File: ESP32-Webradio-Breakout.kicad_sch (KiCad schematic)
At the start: 47 parts, among them J1 AudioJack3, J2 Conn_01x01, J3 Conn_01x02, P1 USB_C_Plug, Q1 BC817, Q2 BC817, Q3 BC817, SW1 RotaryEncoder_Switch, U1 AMS1117-3.3, U2 ESP32-WROOM-32, U3 CH340C, U4 PCF8574TS, U5 DS18B20

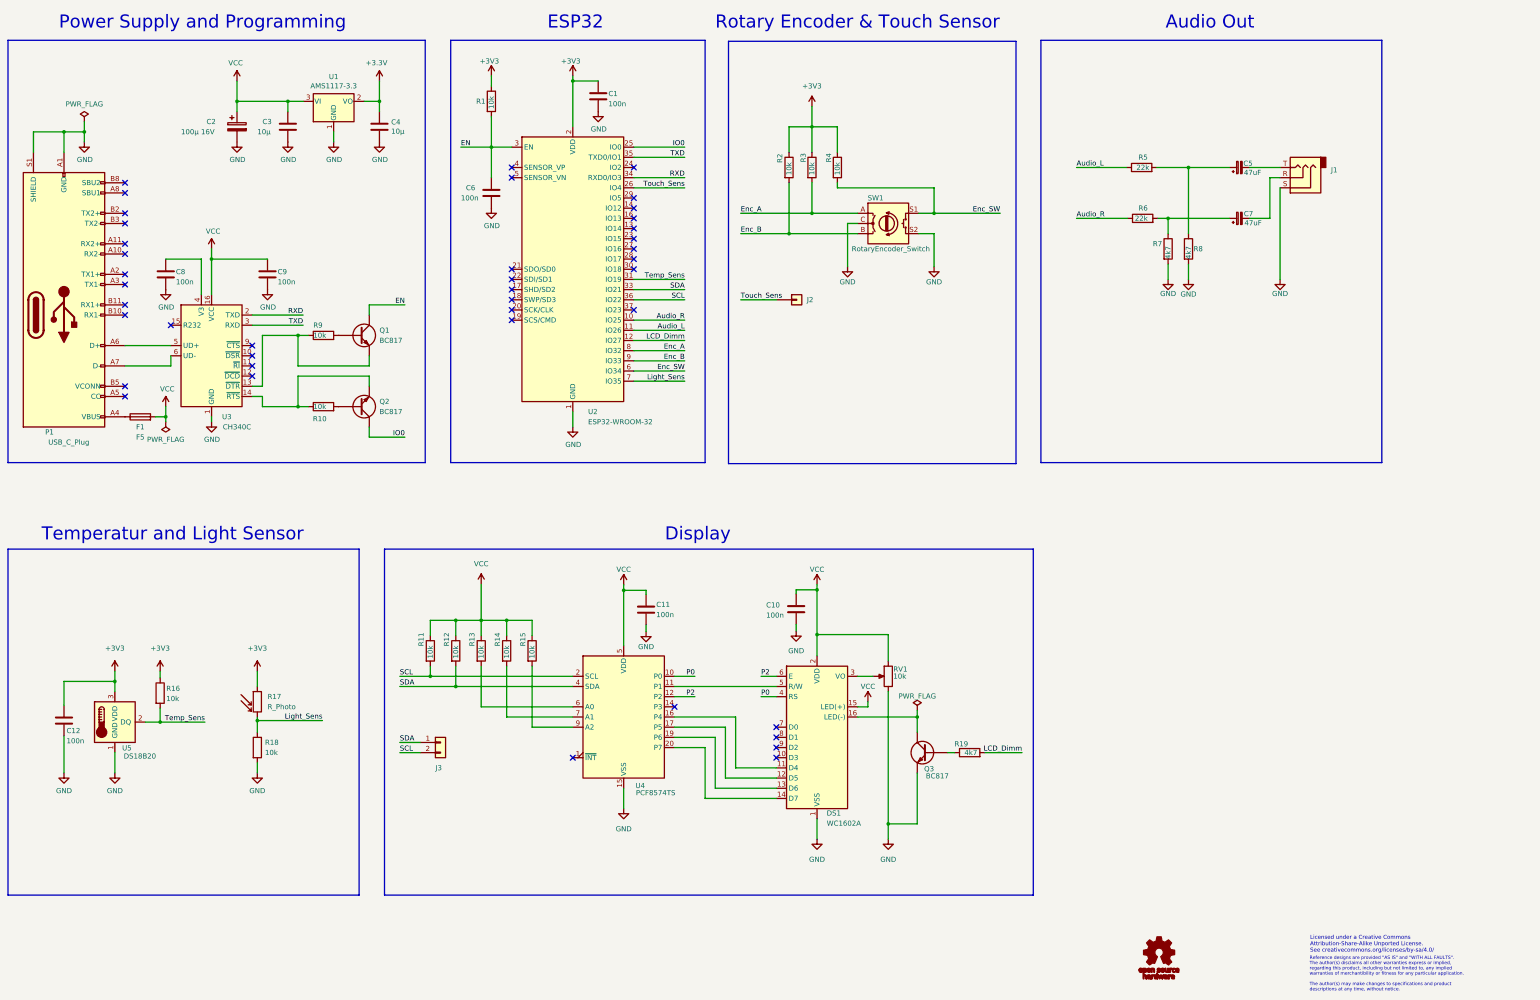
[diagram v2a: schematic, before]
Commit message: Changed USB-C symbol Added 5k1 resistors for 5V handshake
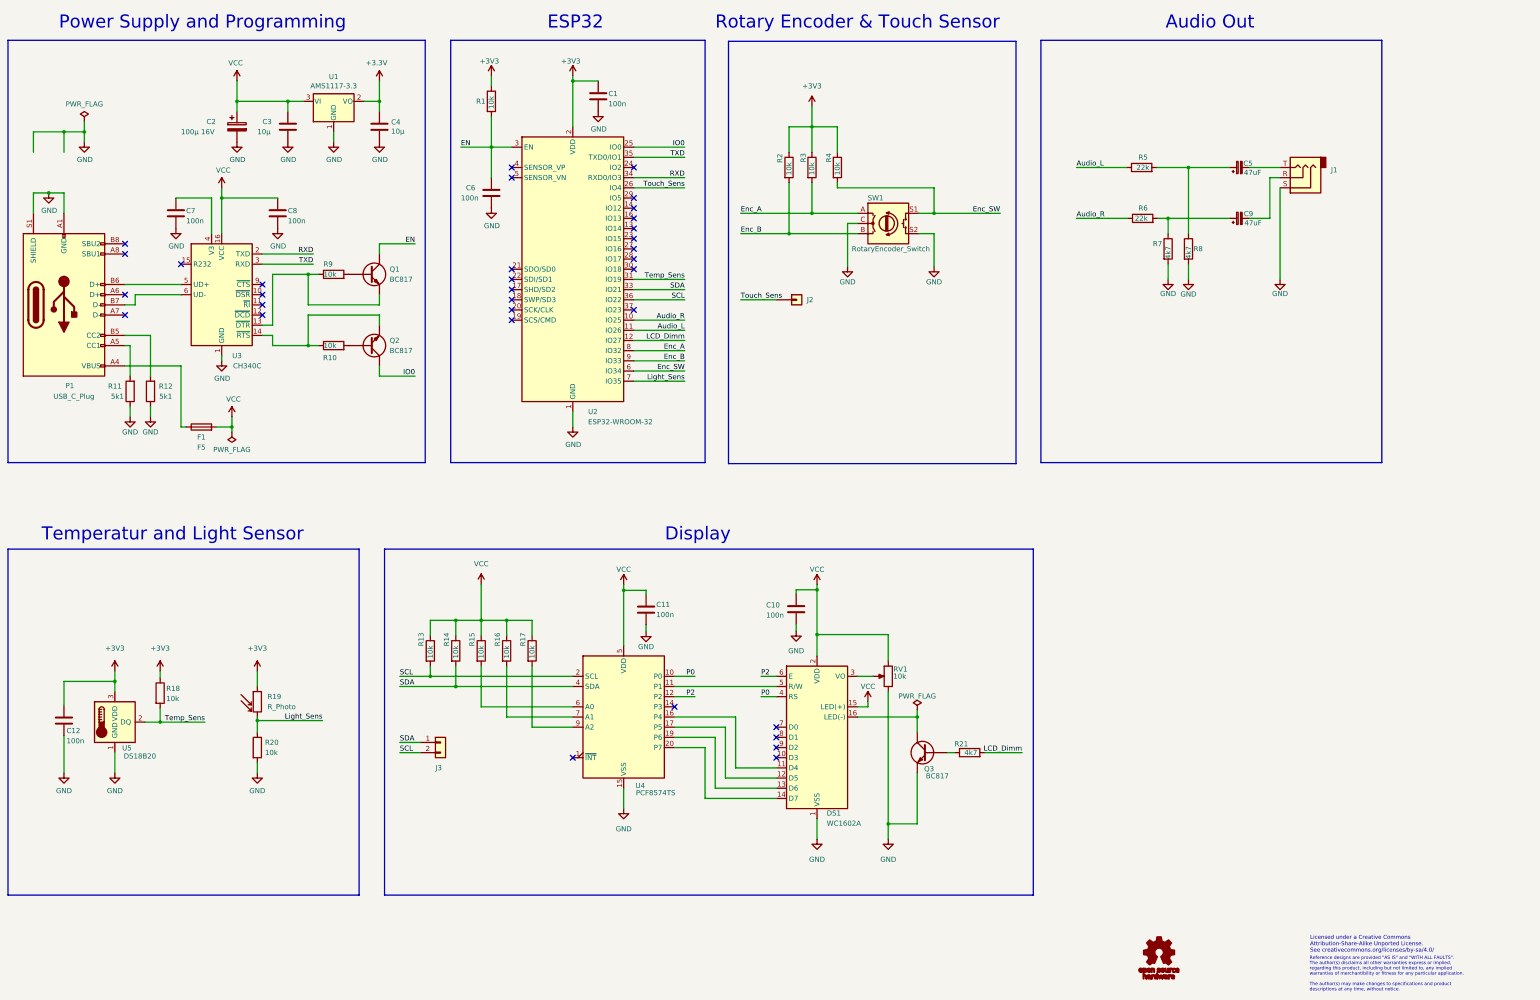
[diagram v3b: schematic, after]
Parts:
- removed P1: USB_C_Plug, Connector_USB:USB_C_Receptacle_XKB_U262-16XN-4BVC11, symbol Connector:USB_C_Plug
- added P1: USB_C_Plug, Connector_USB:USB_C_Receptacle_XKB_U262-16XN-4BVC11, symbol Connector:USB_C_Receptacle_USB2.0
- added R11, R12: 5k1, Resistor_SMD:R_0603_1608Metric, symbol Device:R
- renumbered C8 to C7, C9 to C8, C7 to C9, R11 to R13, R12 to R14, R13 to R15, R14 to R16, R15 to R17, R16 to R18, R17 to R19, R18 to R20, R19 to R21
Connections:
- net GND: now also P1.A1 (GND), P1.A12 (GND), P1.B1 (GND), P1.B12 (GND), P1.S1 (SHIELD), R11.1, R12.1
- net at F1.1: now also P1.A4 (VBUS), P1.A9 (VBUS), P1.B4 (VBUS), P1.B9 (VBUS)
- net at U3.5 (UD+): now also P1.B6 (D+)
- net at U3.6 (UD-): now also P1.B7 (D-)
- new net: P1.A5 (CC1), R11.2
- new net: P1.B5 (CC2), R12.2
- no-connect marks 41 -> 33
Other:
- moved on the sheet: C7, C8, F1, Q1, Q2, R10, R9, U3

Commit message: first routing
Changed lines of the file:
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@@
   (junction (at 149.86 175.26) (diameter 0) (color 0 0 0 0)
   )
-  (junction (at 57.15 53.34) (diameter 0) (color 0 0 0 0)
-  )
   (junction (at 95.25 45.72) (diameter 0) (color 0 0 0 0)
   )
   (junction (at 269.24 73.66) (diameter 0) (color 0 0 0 0)
-  )
-  (junction (at 52.07 53.34) (diameter 0) (color 0 0 0 0)
   )
   (junction (at 64.77 190.5) (diameter 0) (color 0 0 0 0)
@@
     (stroke (width 0) (type default) (color 0 0 0 0))
   )
+  (wire (pts (xy 48.26 61.595) (xy 48.26 68.58))
+    (stroke (width 0) (type default) (color 0 0 0 0))
+  )
   (wire (pts (xy 67.31 106.68) (xy 68.58 106.68))
     (stroke (width 0) (type default) (color 0 0 0 0))
@@
     (stroke (width 0) (type default) (color 0 0 0 0))
   )
+  (wire (pts (xy 48.26 72.39) (xy 48.26 68.58))
+    (stroke (width 0) (type default) (color 0 0 0 0))
+  )
   (wire (pts (xy 217.17 201.93) (xy 217.17 214.63))
     (stroke (width 0) (type default) (color 0 0 0 0))
@@
     (stroke (width 0) (type default) (color 0 0 0 0))
   )
-  (wire (pts (xy 57.15 53.34) (xy 57.15 55.88))
-    (stroke (width 0) (type default) (color 0 0 0 0))
-  )
   (wire (pts (xy 252.73 195.58) (xy 252.73 196.85))
     (stroke (width 0) (type default) (color 0 0 0 0))
@@
   )
   (wire (pts (xy 204.47 191.77) (xy 229.87 191.77))
-    (stroke (width 0) (type default) (color 0 0 0 0))
-  )
-  (wire (pts (xy 52.07 53.34) (xy 52.07 58.42))
     (stroke (width 0) (type default) (color 0 0 0 0))
   )
@@
     (stroke (width 0) (type default) (color 0 0 0 0))
   )
-  (wire (pts (xy 44.45 58.42) (xy 44.45 53.34))
-    (stroke (width 0) (type default) (color 0 0 0 0))
-  )
   (wire (pts (xy 135.89 189.23) (xy 143.51 189.23))
     (stroke (width 0) (type default) (color 0 0 0 0))
@@
     (stroke (width 0) (type default) (color 0 0 0 0))
   )
-  (wire (pts (xy 52.07 53.34) (xy 57.15 53.34))
-    (stroke (width 0) (type default) (color 0 0 0 0))
-  )
   (polyline (pts (xy 148.59 30.48) (xy 148.59 135.89))
     (stroke (width 0) (type default) (color 0 0 0 0))
@@
     (stroke (width 0) (type default) (color 0 0 0 0))
   )
-  (wire (pts (xy 57.15 50.8) (xy 57.15 53.34))
-    (stroke (width 0) (type default) (color 0 0 0 0))
-  )
   (wire (pts (xy 247.65 76.2) (xy 247.65 86.995))
     (stroke (width 0) (type default) (color 0 0 0 0))
@@
   )
   (wire (pts (xy 238.76 52.07) (xy 238.76 58.42))
-    (stroke (width 0) (type default) (color 0 0 0 0))
-  )
-  (wire (pts (xy 44.45 53.34) (xy 52.07 53.34))
     (stroke (width 0) (type default) (color 0 0 0 0))
   )
@@
     (pin "2")
   )
-  (symbol (lib_id "power:PWR_FLAG") (at 57.15 50.8 0) (mirror y) (unit 1)
-    (in_bom yes) (on_board yes)
-    (property "Reference" "#FLG01" (id 0) (at 57.15 48.895 0)
-      (effects (font (size 1.27 1.27)) hide)
-    )
-    (property "Value" "PWR_FLAG" (id 1) (at 57.15 46.4058 0))
-    (property "Footprint" "" (id 2) (at 57.15 50.8 0)
-      (effects (font (size 1.27 1.27)) hide)
-    )
-    (property "Datasheet" "~" (id 3) (at 57.15 50.8 0)
+  (symbol (lib_id "power:PWR_FLAG") (at 48.26 61.595 0) (mirror y) (unit 1)
+    (in_bom yes) (on_board yes)
+    (property "Reference" "#FLG01" (id 0) (at 48.26 59.69 0)
+      (effects (font (size 1.27 1.27)) hide)
+    )
+    (property "Value" "PWR_FLAG" (id 1) (at 48.26 57.2008 0))
+    (property "Footprint" "" (id 2) (at 48.26 61.595 0)
+      (effects (font (size 1.27 1.27)) hide)
+    )
+    (property "Datasheet" "~" (id 3) (at 48.26 61.595 0)
       (effects (font (size 1.27 1.27)) hide)
     )
@@
     (pin "8")
     (pin "9")
-  )
-  (symbol (lib_id "power:GND") (at 57.15 55.88 0) (unit 1)
-    (in_bom yes) (on_board yes)
-    (property "Reference" "#PWR07" (id 0) (at 57.15 62.23 0)
-      (effects (font (size 1.27 1.27)) hide)
-    )
-    (property "Value" "GND" (id 1) (at 57.277 60.2742 0))
-    (property "Footprint" "" (id 2) (at 57.15 55.88 0)
-      (effects (font (size 1.27 1.27)) hide)
-    )
-    (property "Datasheet" "" (id 3) (at 57.15 55.88 0)
-      (effects (font (size 1.27 1.27)) hide)
-    )
-    (pin "1")
   )
   (symbol (lib_id "power:VCC") (at 91.44 67.31 0) (unit 1)
@@
     (pin "2")
   )
-  (symbol (lib_id "power:GND") (at 48.26 68.58 0) (unit 1)
-    (in_bom yes) (on_board yes)
-    (property "Reference" "#PWR013" (id 0) (at 48.26 74.93 0)
-      (effects (font (size 1.27 1.27)) hide)
-    )
-    (property "Value" "GND" (id 1) (at 48.387 72.9742 0))
-    (property "Footprint" "" (id 2) (at 48.26 68.58 0)
-      (effects (font (size 1.27 1.27)) hide)
-    )
-    (property "Datasheet" "" (id 3) (at 48.26 68.58 0)
+  (symbol (lib_id "power:GND") (at 48.26 72.39 0) (unit 1)
+    (in_bom yes) (on_board yes)
+    (property "Reference" "#PWR013" (id 0) (at 48.26 78.74 0)
+      (effects (font (size 1.27 1.27)) hide)
+    )
+    (property "Value" "GND" (id 1) (at 48.387 76.7842 0))
+    (property "Footprint" "" (id 2) (at 48.26 72.39 0)
+      (effects (font (size 1.27 1.27)) hide)
+    )
+    (property "Datasheet" "" (id 3) (at 48.26 72.39 0)
       (effects (font (size 1.27 1.27)) hide)
     )
@@
       (reference "#PWR06") (unit 1) (value "GND") (footprint "")
     )
-    (path "/61d6f09d-0968-4b05-bb39-9c26a7587ffc"
-      (reference "#PWR07") (unit 1) (value "GND") (footprint "")
-    )
     (path "/90bf5586-80a1-4437-ad00-cee07aea1480"

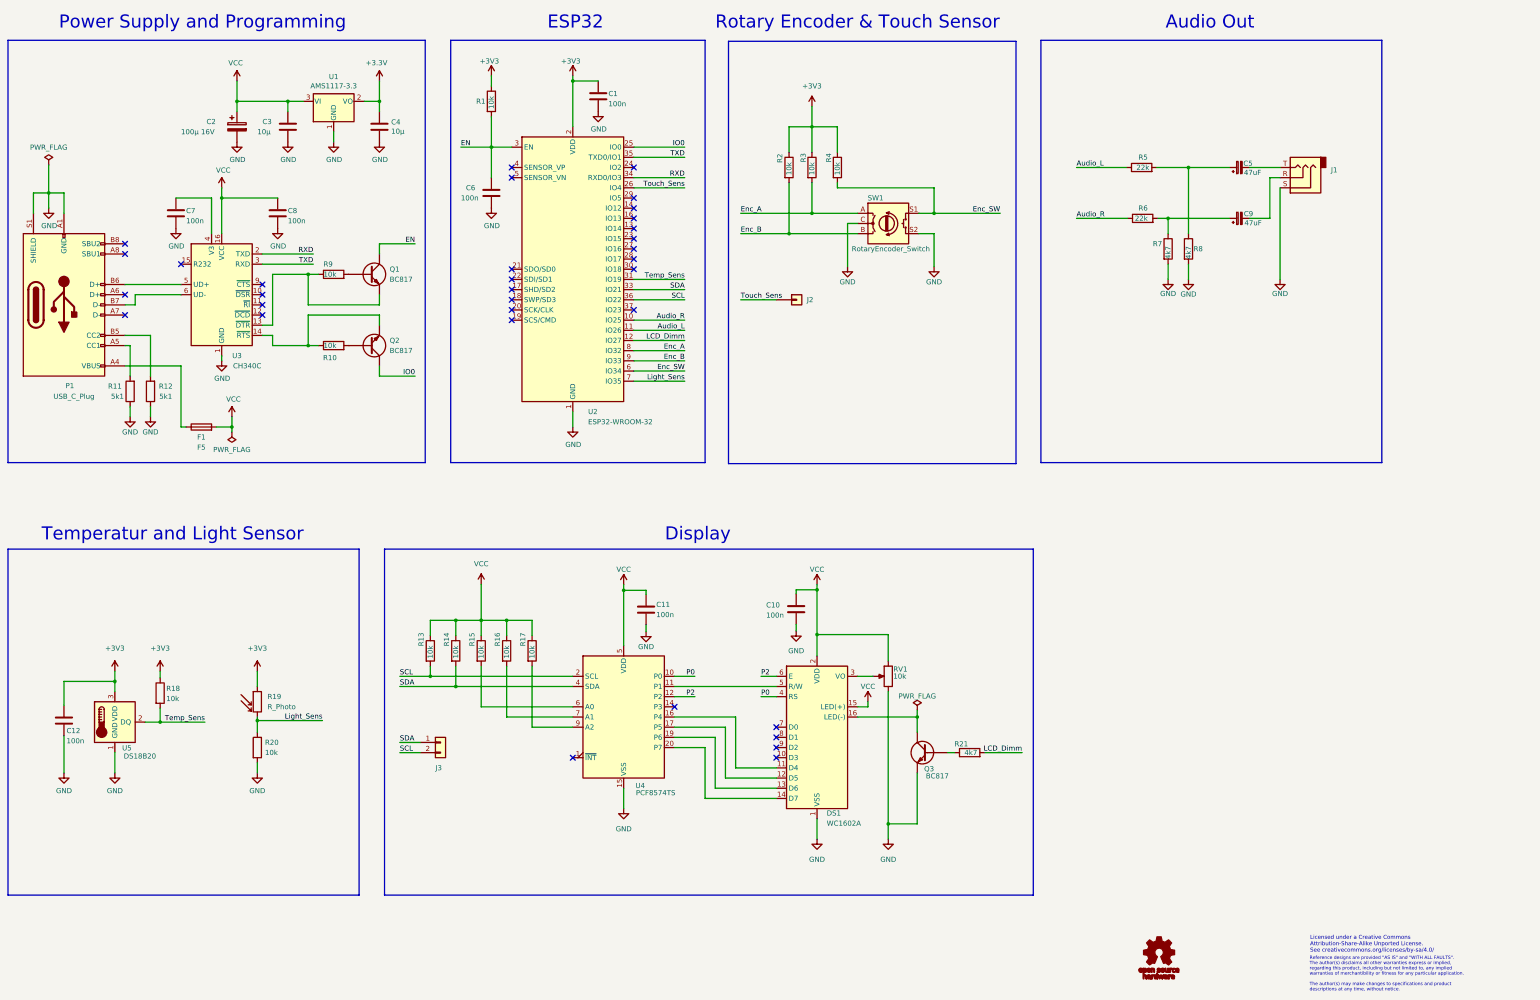
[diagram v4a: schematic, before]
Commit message: Added MicroSD cardreader
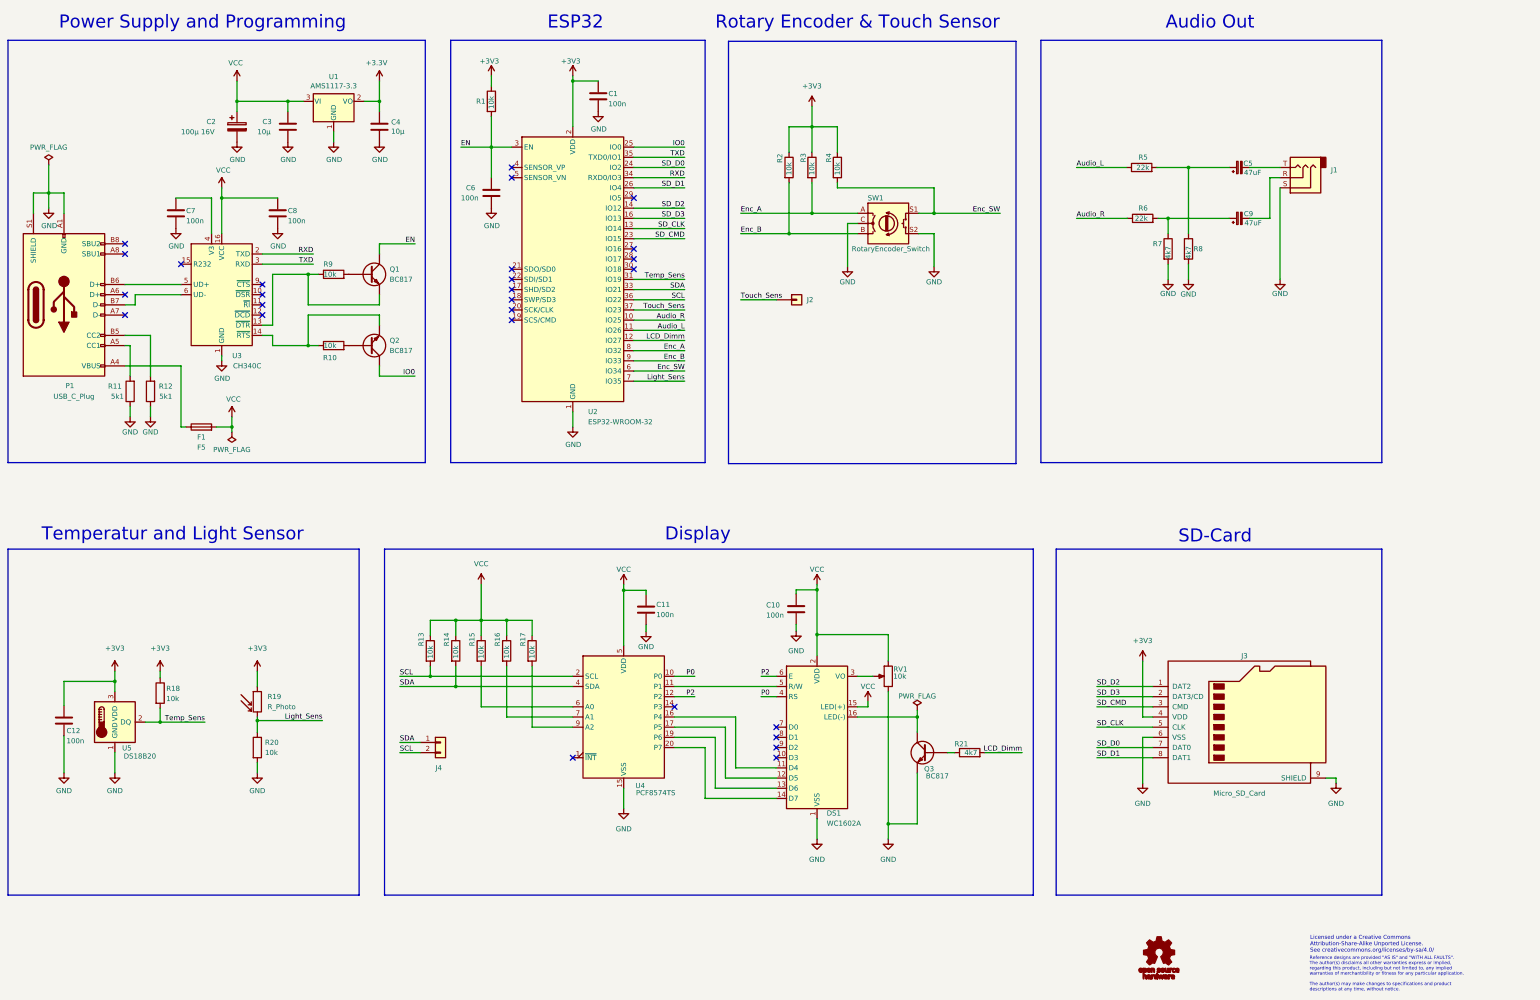
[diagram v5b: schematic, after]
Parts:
- added J3: Micro_SD_Card, Connector_Card:microSD_HC_Wuerth_693072010801, symbol Connector:Micro_SD_Card
- renumbered J3 to J4
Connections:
- net +3V3: now also J3.4 (VDD)
- net GND: now also J3.6 (VSS), J3.9 (SHIELD)
- net Touch_Sens: now also U2.37 (IO23); no longer U2.26 (IO4)
- net SD_CLK: now reaches U2.13 (IO14)
- net SD_CLK: now also J3.5 (CLK)
- net SD_D2: now reaches U2.14 (IO12)
- net SD_D2: now also J3.1 (DAT2)
- net SD_D3: now reaches U2.16 (IO13)
- net SD_D3: now also J3.2 (DAT3/CD)
- net SD_CMD: now reaches U2.23 (IO15)
- net SD_CMD: now also J3.3 (CMD)
- net SD_D0: now reaches U2.24 (IO2)
- net SD_D0: now also J3.7 (DAT0)
- new net SD_D1: J3.8 (DAT1), U2.26 (IO4)
- no-connect marks 33 -> 27
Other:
- note added: "SD-Card"
